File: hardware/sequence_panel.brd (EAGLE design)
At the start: 209.6 x 149.9 mm, 10 parts

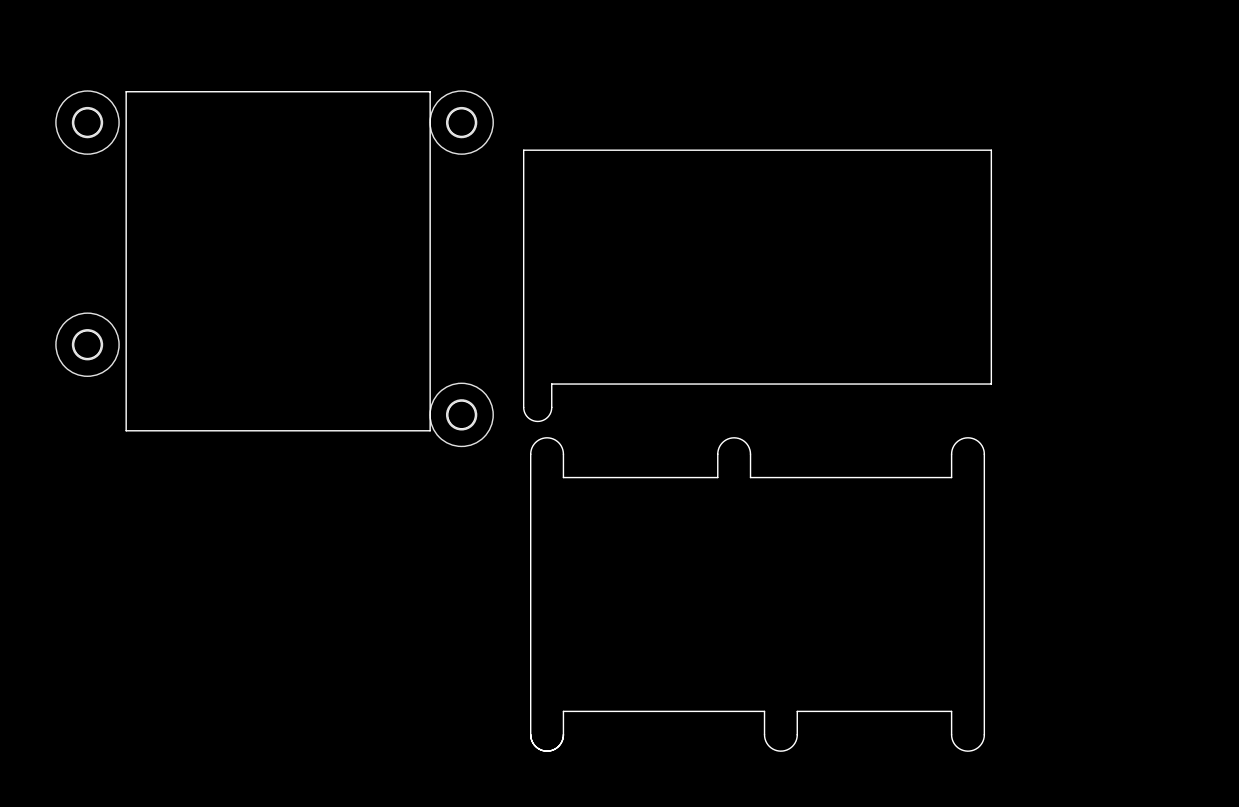
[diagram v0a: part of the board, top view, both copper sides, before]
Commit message: Added methods to add new event to pattern
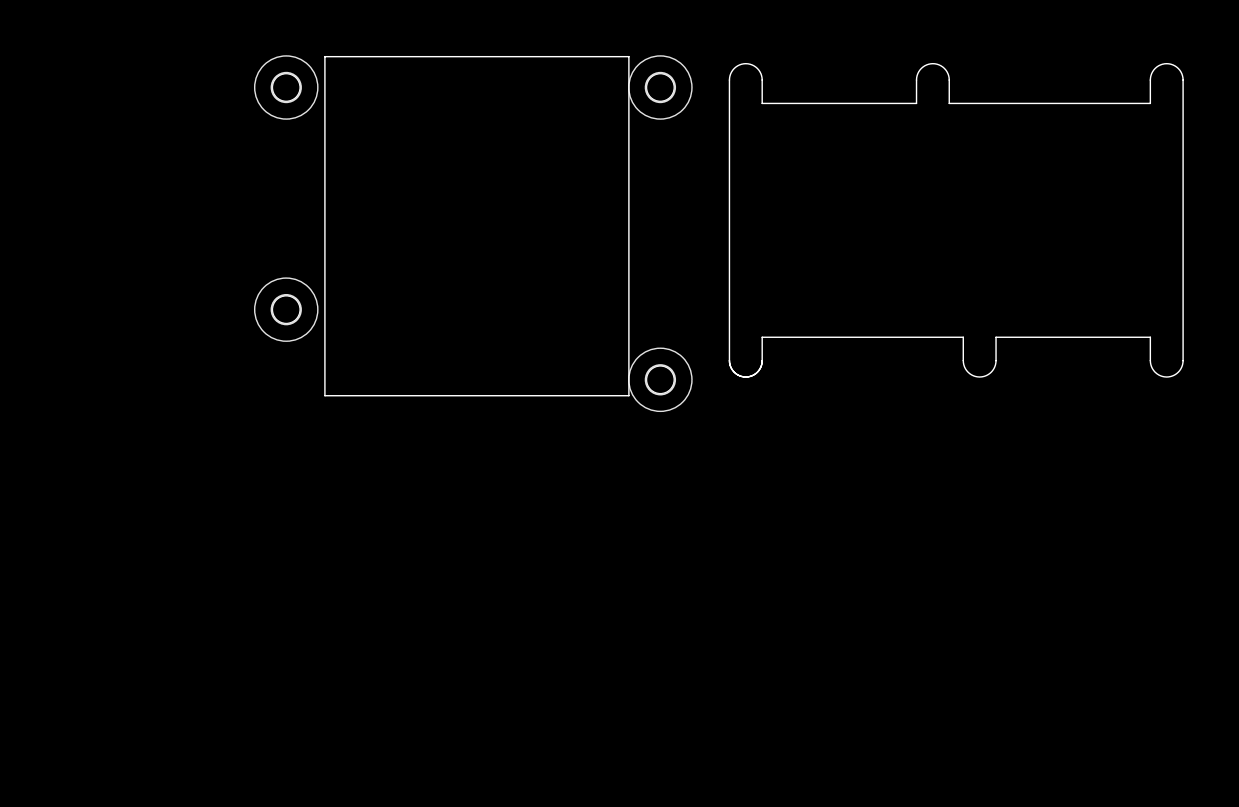
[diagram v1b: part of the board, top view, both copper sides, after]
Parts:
- moved U$16 21.9 mm to (55.5, 81.7)
- moved U$7 21.9 mm to (55.5, 105.9)
- moved U$15 21.9 mm to (96.1, 74.1)
- moved U$2 21.9 mm to (96.1, 105.9)
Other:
- outline, holes or cut-outs redrawn
